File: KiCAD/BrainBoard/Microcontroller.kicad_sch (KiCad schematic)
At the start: 17 parts, among them J2 USB4216-03-A, SW1 SW_SPDT, U6 STM32F303CCTx, Y1 NX3225SA-32.000MHZ-STD-CSR-1

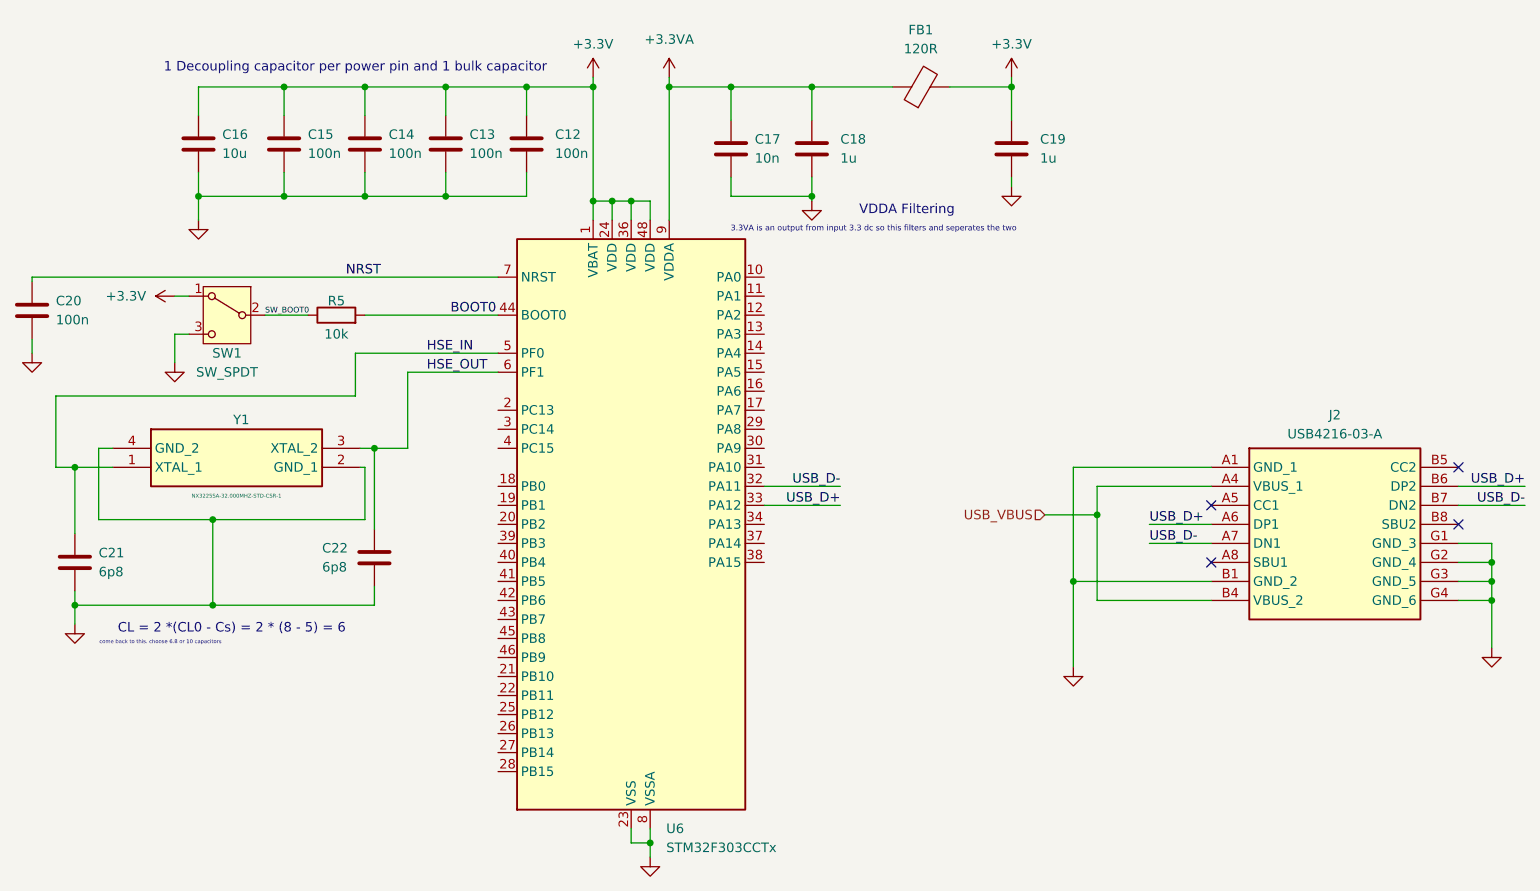
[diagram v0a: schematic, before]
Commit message: fix: Make DRC happy
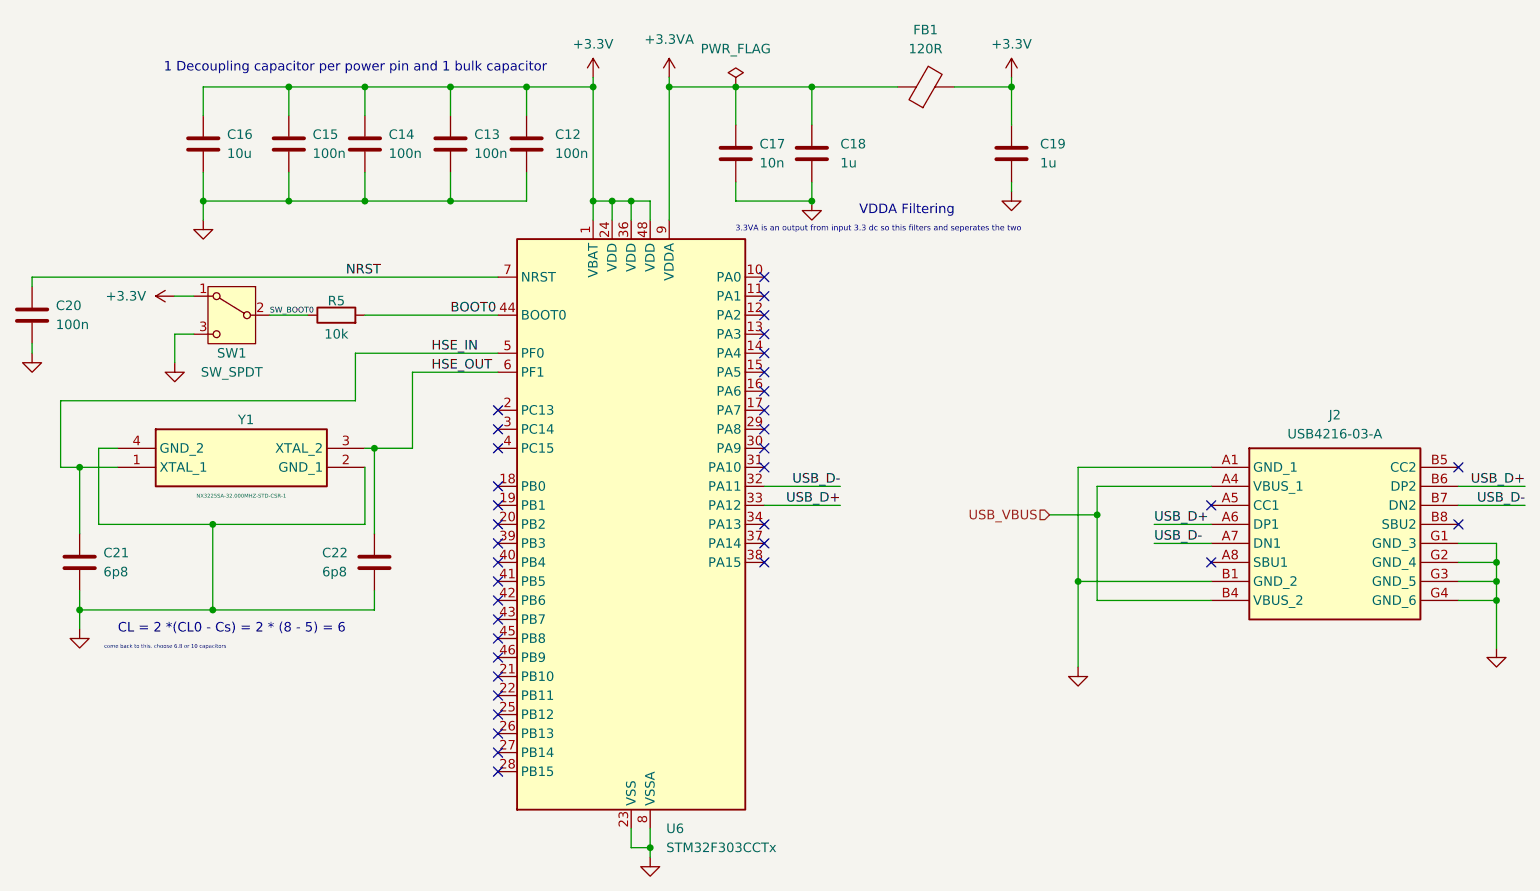
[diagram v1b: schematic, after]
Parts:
- J2: footprint USB421603A -> SamacSys_Parts:USB421603A
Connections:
- no-connect marks 4 -> 37
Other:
- moved on the sheet: C13, C15, C16, C17, C18, C19, C20, C21, C22, FB1, SW1, Y1

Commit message: Added and finalized GPIO and PWM pinouts
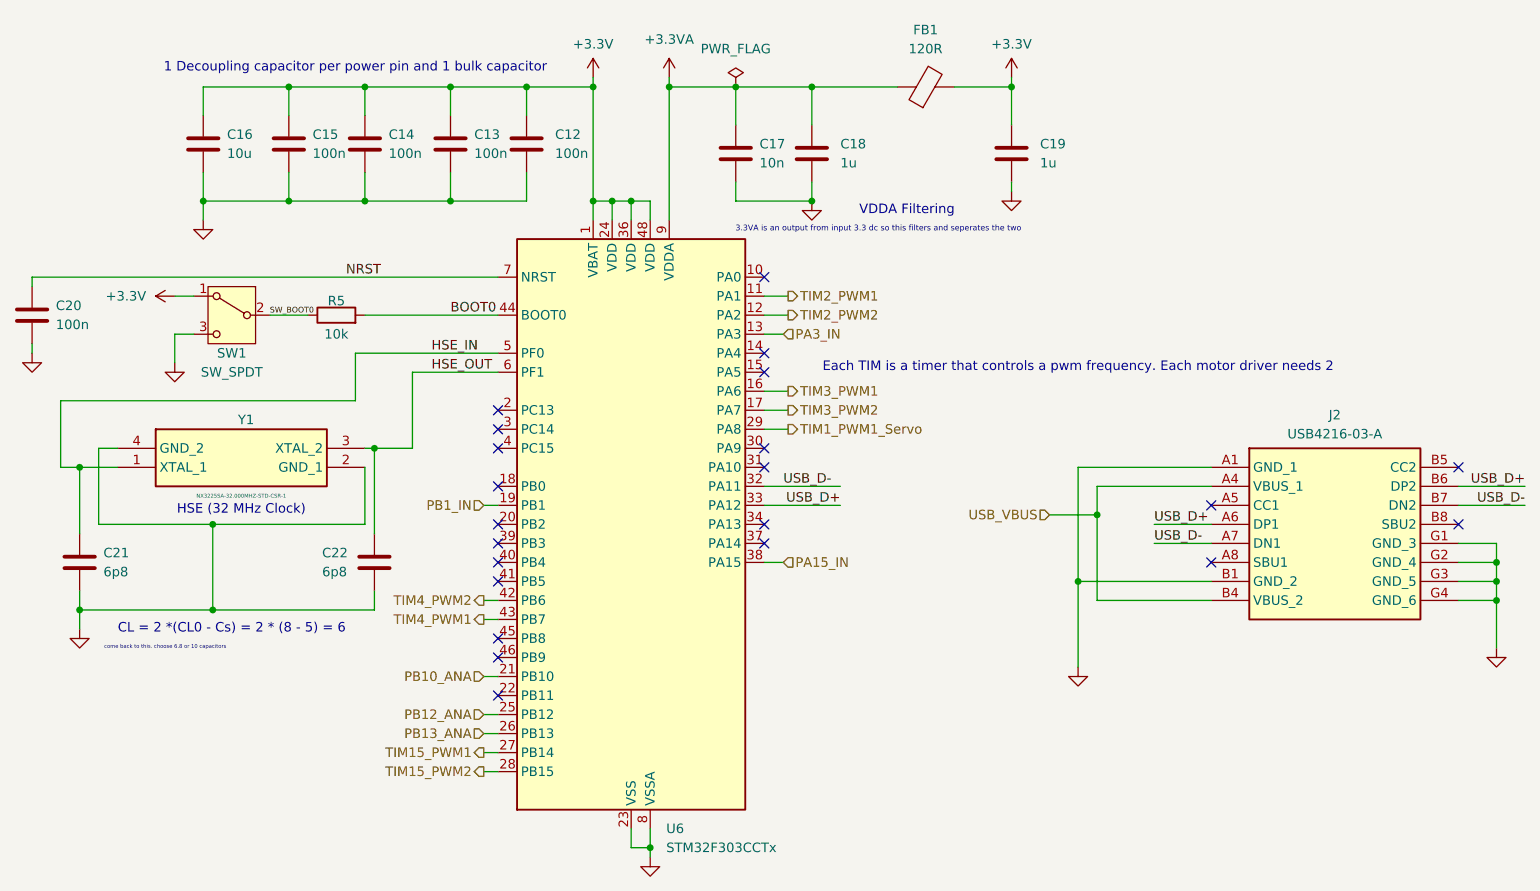
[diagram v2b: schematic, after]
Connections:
- net TIM2_PWM1: now reaches U6.11 (PA1)
- net TIM2_PWM2: now reaches U6.12 (PA2)
- net PA3_IN: now reaches U6.13 (PA3)
- net TIM3_PWM1: now reaches U6.16 (PA6)
- net TIM3_PWM2: now reaches U6.17 (PA7)
- net PB1_IN: now reaches U6.19 (PB1)
- net PB10_ANA: now reaches U6.21 (PB10)
- net PB12_ANA: now reaches U6.25 (PB12)
- net PB13_ANA: now reaches U6.26 (PB13)
- net TIM15_PWM1: now reaches U6.27 (PB14)
- net TIM15_PWM2: now reaches U6.28 (PB15)
- net TIM1_PWM1_Servo: now reaches U6.29 (PA8)
- net PA15_IN: now reaches U6.38 (PA15)
- net TIM4_PWM2: now reaches U6.42 (PB6)
- net TIM4_PWM1: now reaches U6.43 (PB7)
- no-connect marks 37 -> 22
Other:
- note added: "Each TIM is a timer that controls a pwm frequency. Each motor driver needs 2"
- note added: "HSE (32 MHz Clock)"

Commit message: feat: battery input
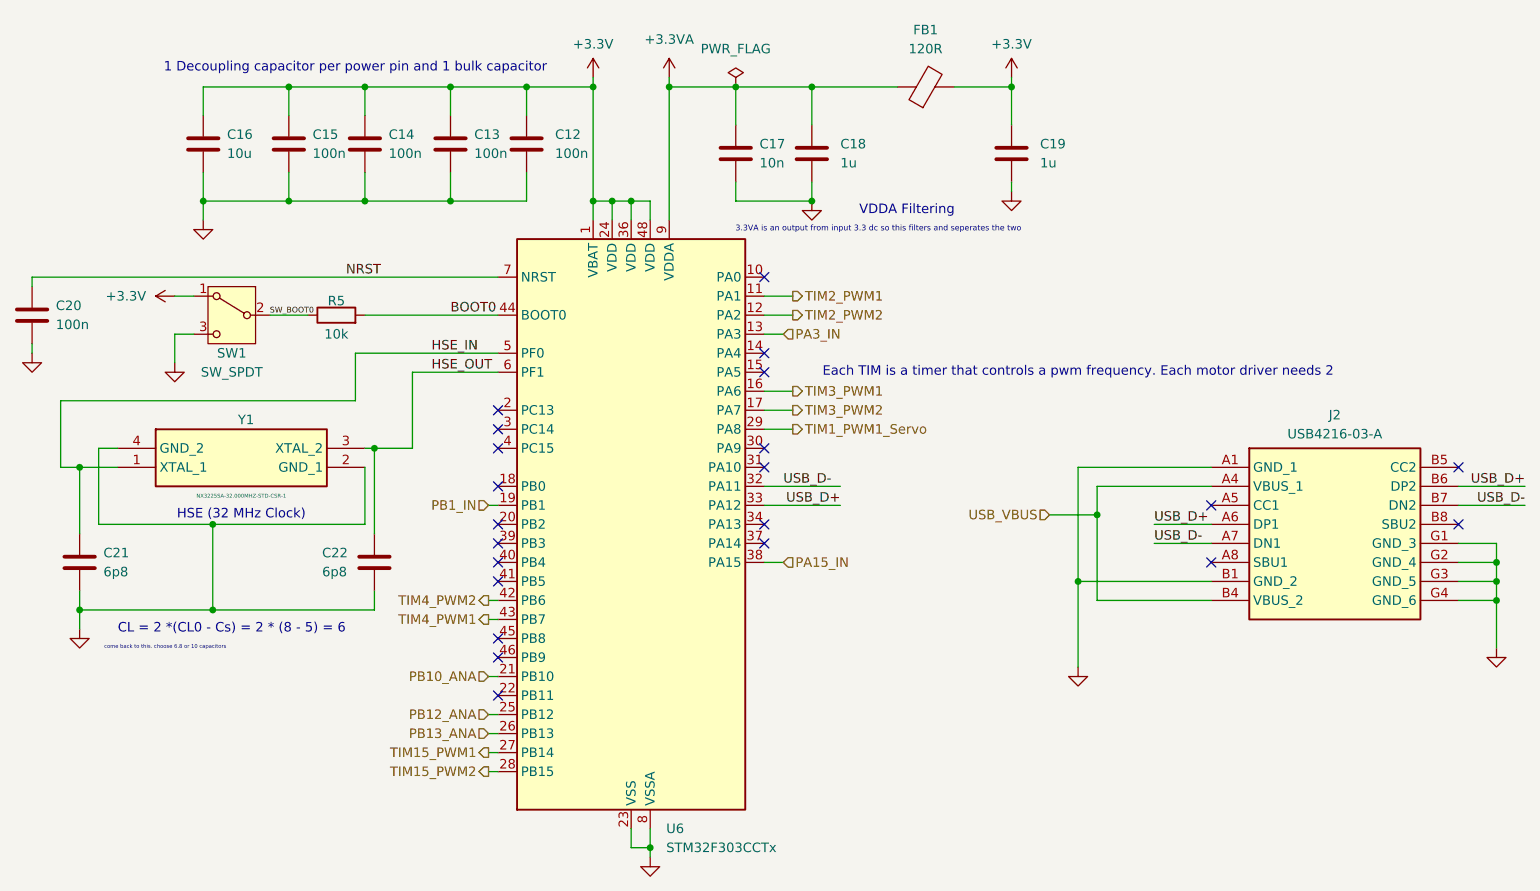
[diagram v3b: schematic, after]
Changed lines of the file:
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@@
 	(text "HSE (32 MHz Clock)\n"
 		(exclude_from_sim no)
-		(at 92.71 83.185 0)
+		(at 92.71 83.82 0)
 		(effects
 			(font
@@
 	(text "Each TIM is a timer that controls a pwm frequency. Each motor driver needs 2"
 		(exclude_from_sim no)
-		(at 204.47 64.135 0)
+		(at 204.47 64.77 0)
 		(effects
 			(font
@@
 	(wire
 		(pts
-			(xy 125.095 105.41) (xy 127 105.41)
-		)
-		(stroke
-			(width 0)
-			(type default)
-		)
-	)
-	(wire
-		(pts
-			(xy 125.095 113.03) (xy 127 113.03)
+			(xy 125.73 105.41) (xy 127 105.41)
+		)
+		(stroke
+			(width 0)
+			(type default)
+		)
+	)
+	(wire
+		(pts
+			(xy 125.73 113.03) (xy 127 113.03)
 		)
 		(stroke
@@
 	(wire
 		(pts
-			(xy 162.56 57.15) (xy 165.735 57.15)
+			(xy 162.56 57.15) (xy 166.37 57.15)
 		)
 		(stroke
@@
 	(wire
 		(pts
-			(xy 125.095 97.79) (xy 127 97.79)
-		)
-		(stroke
-			(width 0)
-			(type default)
-		)
-	)
-	(wire
-		(pts
-			(xy 125.095 82.55) (xy 127 82.55)
+			(xy 125.73 97.79) (xy 127 97.79)
+		)
+		(stroke
+			(width 0)
+			(type default)
+		)
+	)
+	(wire
+		(pts
+			(xy 125.73 82.55) (xy 127 82.55)
 		)
 		(stroke
@@
 	(wire
 		(pts
-			(xy 125.095 115.57) (xy 127 115.57)
+			(xy 125.73 115.57) (xy 127 115.57)
 		)
 		(stroke
@@
 	(wire
 		(pts
-			(xy 162.56 54.61) (xy 165.735 54.61)
-		)
-		(stroke
-			(width 0)
-			(type default)
-		)
-	)
-	(wire
-		(pts
-			(xy 125.095 110.49) (xy 127 110.49)
+			(xy 162.56 54.61) (xy 166.37 54.61)
+		)
+		(stroke
+			(width 0)
+			(type default)
+		)
+	)
+	(wire
+		(pts
+			(xy 125.73 110.49) (xy 127 110.49)
 		)
 		(stroke
@@
 	(wire
 		(pts
-			(xy 162.56 69.85) (xy 165.735 69.85)
+			(xy 162.56 69.85) (xy 166.37 69.85)
 		)
 		(stroke
@@
 	(wire
 		(pts
-			(xy 162.56 72.39) (xy 165.735 72.39)
+			(xy 162.56 72.39) (xy 166.37 72.39)
 		)
 		(stroke
@@
 	(wire
 		(pts
-			(xy 125.095 95.25) (xy 127 95.25)
+			(xy 125.73 95.25) (xy 127 95.25)
 		)
 		(stroke
@@
 	(wire
 		(pts
-			(xy 162.56 67.31) (xy 165.735 67.31)
+			(xy 162.56 67.31) (xy 166.37 67.31)
 		)
 		(stroke
@@
 	(wire
 		(pts
-			(xy 125.095 118.11) (xy 127 118.11)
+			(xy 125.73 118.11) (xy 127 118.11)
 		)
 		(stroke
@@
 	(hierarchical_label "PB12_ANA"
 		(shape input)
-		(at 125.095 110.49 180)
+		(at 125.73 110.49 180)
 		(effects
 			(font
@@
 	(hierarchical_label "TIM3_PWM1"
 		(shape output)
-		(at 165.735 67.31 0)
+		(at 166.37 67.31 0)
 		(effects
 			(font
@@
 	(hierarchical_label "PB1_IN"
 		(shape input)
-		(at 125.095 82.55 180)
+		(at 125.73 82.55 180)
 		(effects
 			(font
@@
 	(hierarchical_label "TIM2_PWM1"
 		(shape output)
-		(at 165.735 54.61 0)
+		(at 166.37 54.61 0)
 		(effects
 			(font
@@
 	(hierarchical_label "TIM3_PWM2"
 		(shape output)
-		(at 165.735 69.85 0)
+		(at 166.37 69.85 0)
 		(effects
 			(font
@@
 	(hierarchical_label "TIM1_PWM1_Servo"
 		(shape output)
-		(at 165.735 72.39 0)
+		(at 166.37 72.39 0)
 		(effects
 			(font
@@
 	(hierarchical_label "PB13_ANA"
 		(shape input)
-		(at 125.095 113.03 180)
+		(at 125.73 113.03 180)
 		(effects
 			(font
@@
 	(hierarchical_label "TIM2_PWM2"
 		(shape output)
-		(at 165.735 57.15 0)
+		(at 166.37 57.15 0)
 		(effects
 			(font
@@
 	(hierarchical_label "TIM15_PWM2"
 		(shape output)
-		(at 125.095 118.11 180)
+		(at 125.73 118.11 180)
 		(effects
 			(font
@@
 	(hierarchical_label "TIM15_PWM1"
 		(shape output)
-		(at 125.095 115.57 180)
+		(at 125.73 115.57 180)
 		(effects
 			(font
@@
 	(hierarchical_label "TIM4_PWM2"
 		(shape output)
-		(at 125.095 95.25 180)
+		(at 125.73 95.25 180)
 		(effects
 			(font
@@
 	(hierarchical_label "PB10_ANA"
 		(shape input)
-		(at 125.095 105.41 180)
+		(at 125.73 105.41 180)
 		(effects
 			(font
@@
 	(hierarchical_label "TIM4_PWM1"
 		(shape output)
-		(at 125.095 97.79 180)
-		(effects
-			(font
+		(at 125.73 97.79 180)
+		(effects
+			(font
